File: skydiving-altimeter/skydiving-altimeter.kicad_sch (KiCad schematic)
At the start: 2 parts, among them J2 Battery JST Connector, J3 SPST Power Switch Wire Connec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

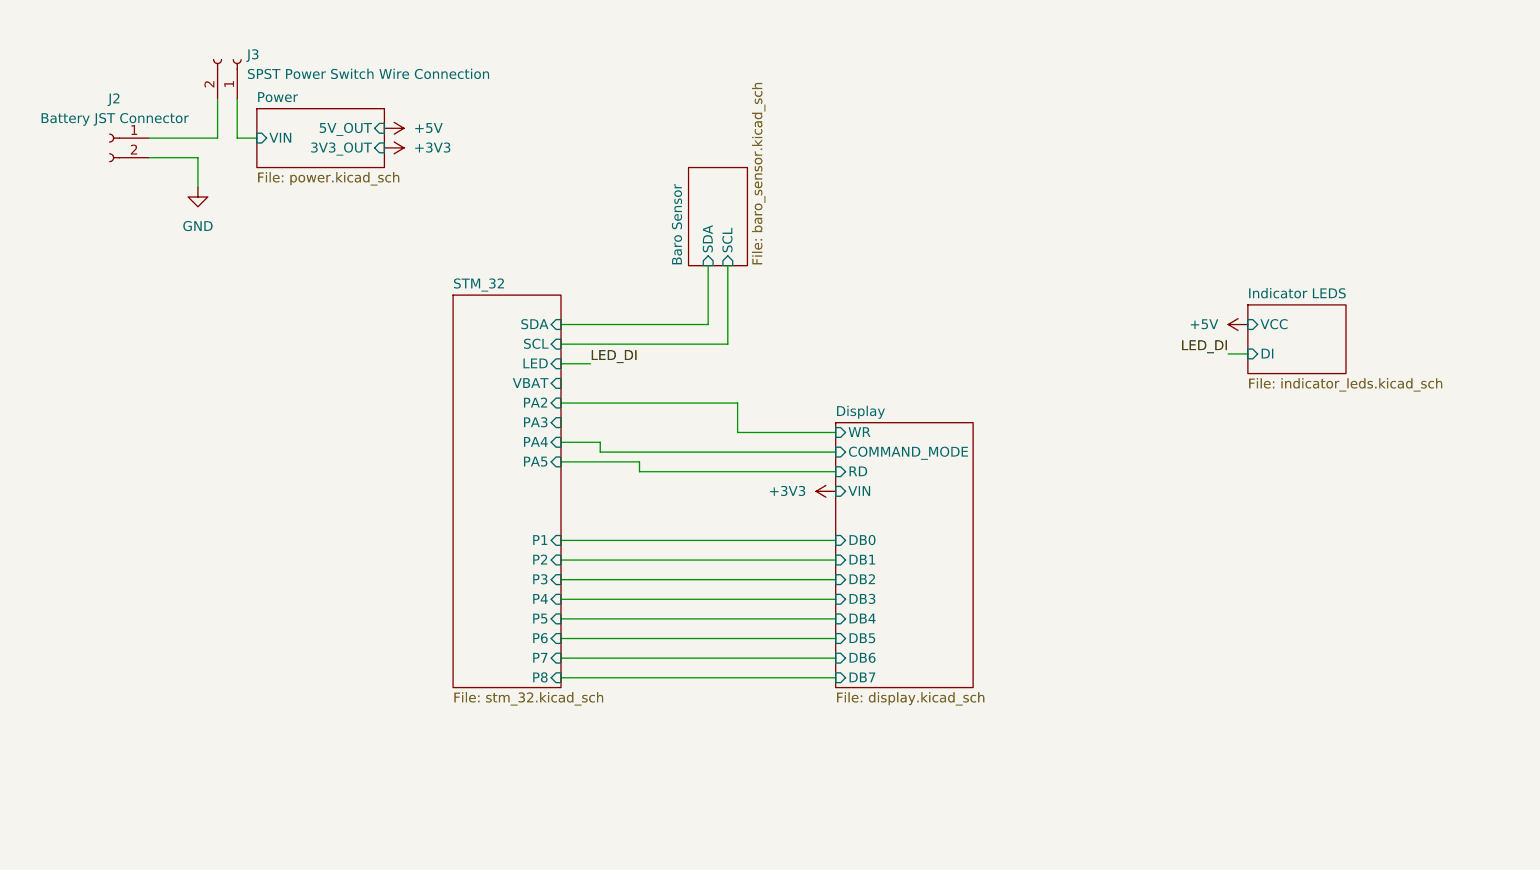
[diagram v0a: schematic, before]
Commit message: Started rerouting
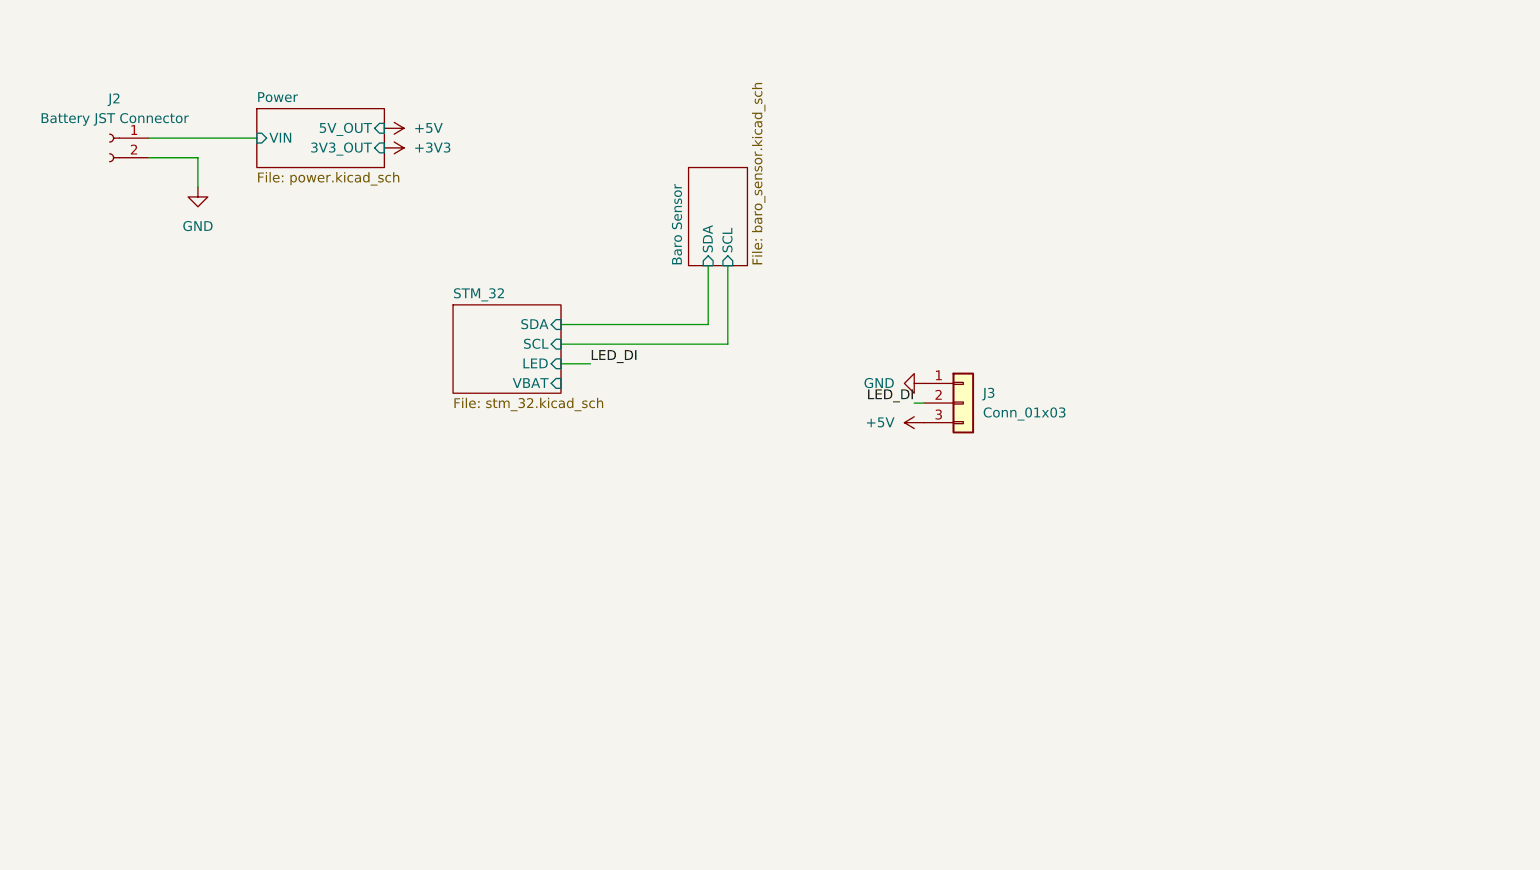
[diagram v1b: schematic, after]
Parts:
- removed J3: SPST Power Switch Wire Connection, Connector_PinHeader_2.54mm:PinHeader_1x02_P2.54mm_Vertical, symbol Connector:Conn_01x02_Female
- added J3: Conn_01x03, Connector_PinHeader_2.54mm:PinHeader_1x03_P2.54mm_Vertical, symbol Connector_Generic:Conn_01x03
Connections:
- net +5V: now also J3.3 (Pin_3)
- net GND: now also J3.1 (Pin_1)
- net LED_DI: now also J3.2 (Pin_2)
- net Power/VIN: now also J2.1 (Pin_1)
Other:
- removed sheet Display
- removed sheet Indicator LEDS
- sheet STM_32 ports: added none; removed P1, P2, P3, P4, P5, P6, P7, P8, PA2, PA3, PA4, PA5

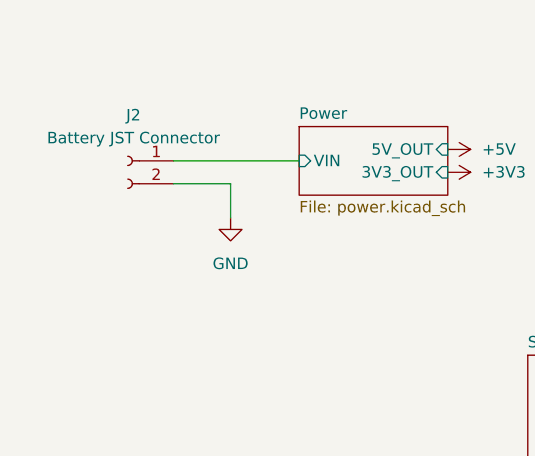
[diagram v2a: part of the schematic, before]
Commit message: Began adding 10 ohm current limiting resistors
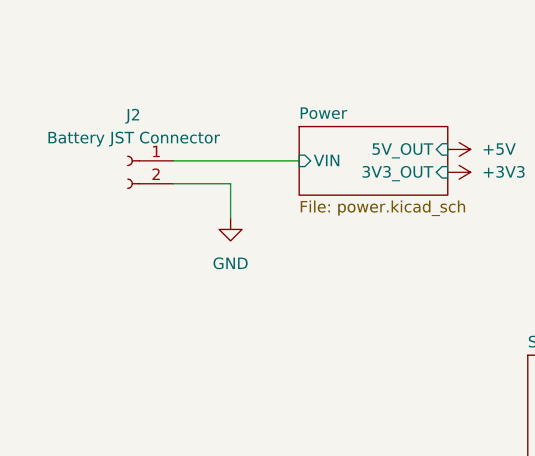
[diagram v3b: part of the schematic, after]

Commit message: Mostly rerouted
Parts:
- added U6, U7: CAT24M01W, Package_SO:SOIC-8_3.9x4.9mm_P1.27mm, symbol Memory_EEPROM:CAT24M01W
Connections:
- net +3V3: now also U6.8 (VCC), U7.2 (A1), U7.8 (VCC)
- net Baro Sensor/SCL: now also U6.6 (SCL), U7.6 (SCL)
- net Baro Sensor/SDA: now also U6.5 (SDA), U7.5 (SDA)
- net GND: now also U6.4 (GND), U7.4 (GND)
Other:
- note added: "1MBit EEPROM"
